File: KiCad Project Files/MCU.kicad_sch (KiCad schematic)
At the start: 25 parts, among them SW1 Boot, SW2 Reset, U1 RP2040, U2 W25Q128JVS, Y1 12MHz

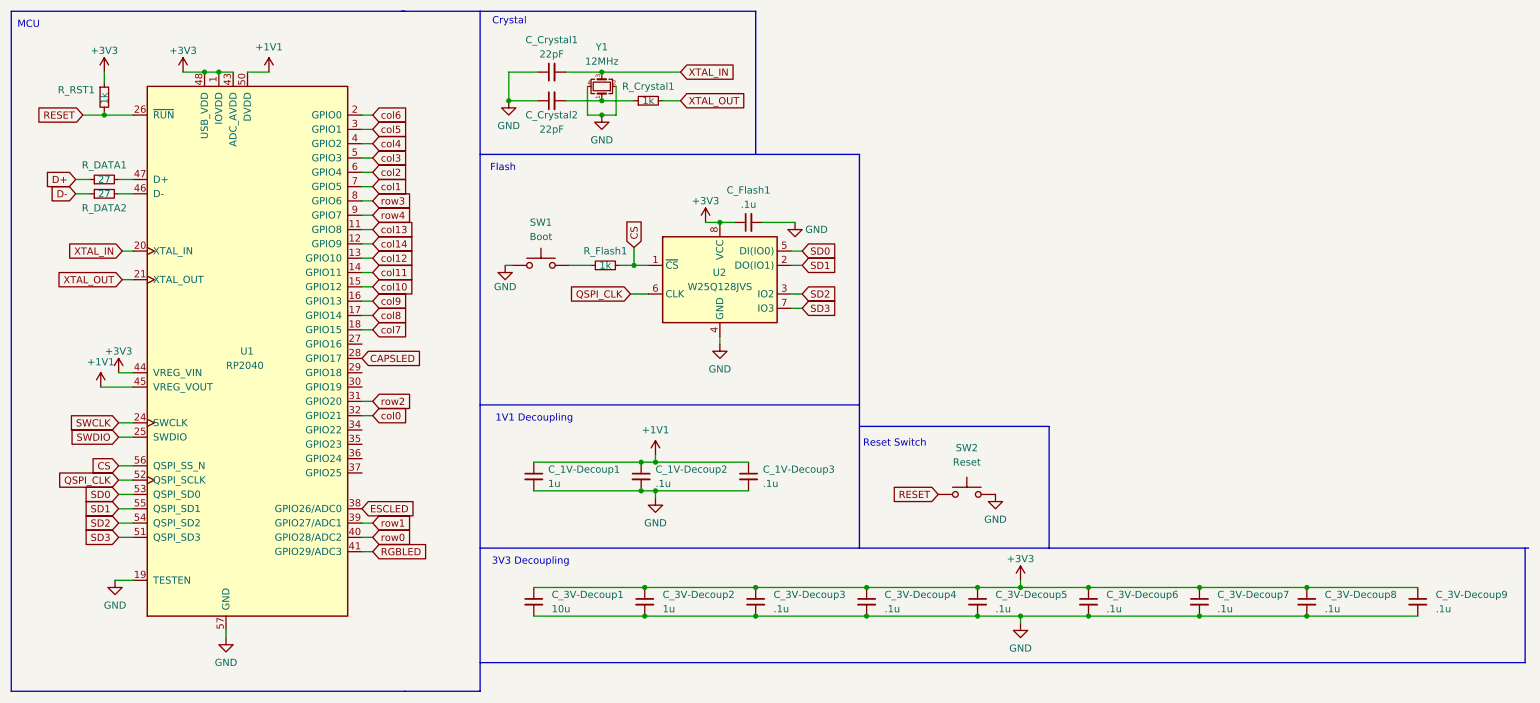
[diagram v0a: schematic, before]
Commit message: Initial Modifications
Summary of changes from original SST60:
-Removes extraneous keys, opting for ANSI-only, split right shift, split Backspace, 7U space bar, stepped caps lock.
-Switched from MX-ANSI hybrid to MX-only
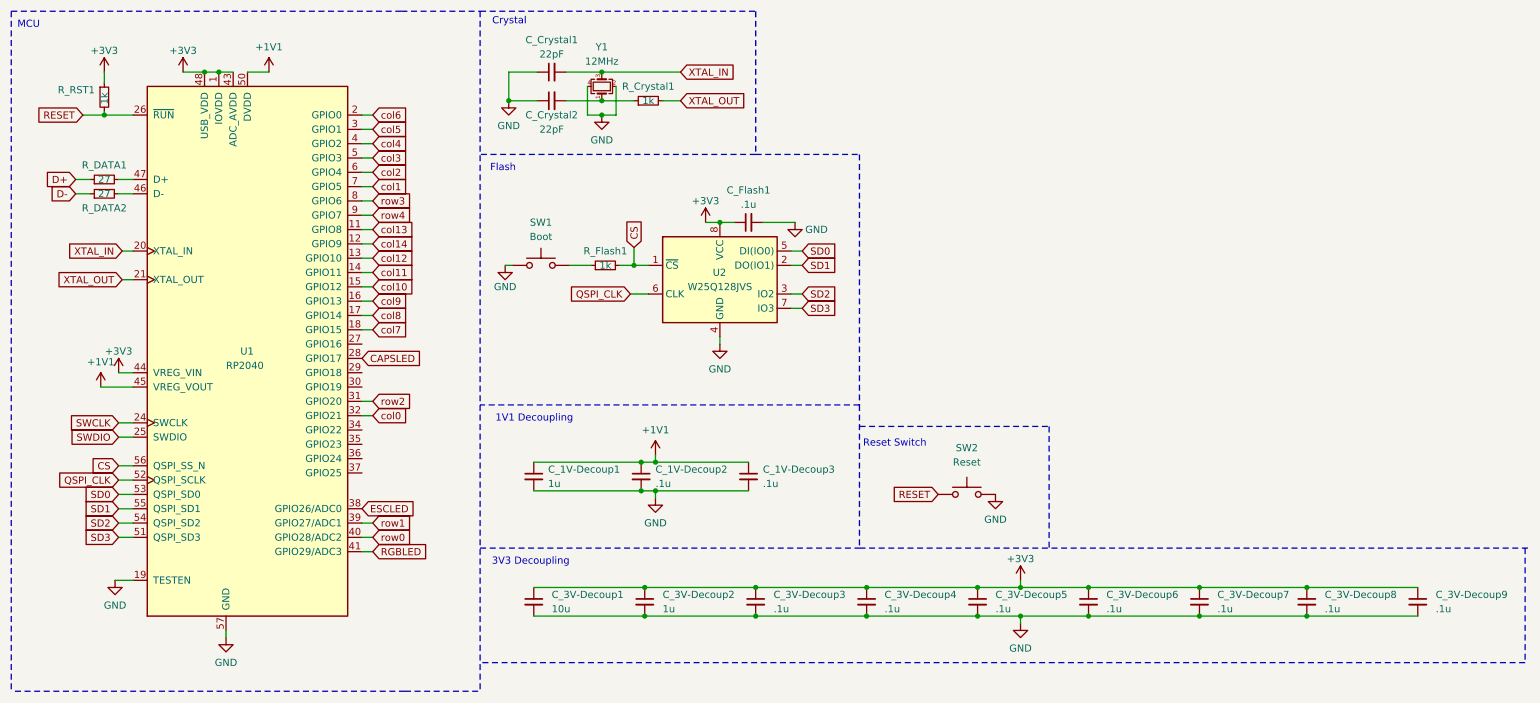
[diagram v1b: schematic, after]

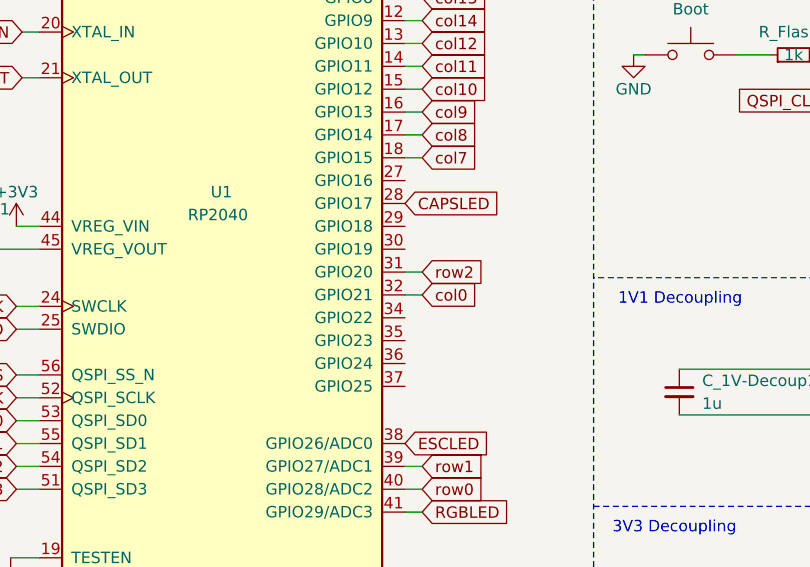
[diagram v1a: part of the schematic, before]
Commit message: Error Cleanup
Resolved all errors in sch, and most errors in pcb, except "intentional" ones concerning H1.
Will readdress rule changes and violations once attempting to submit to fab house.
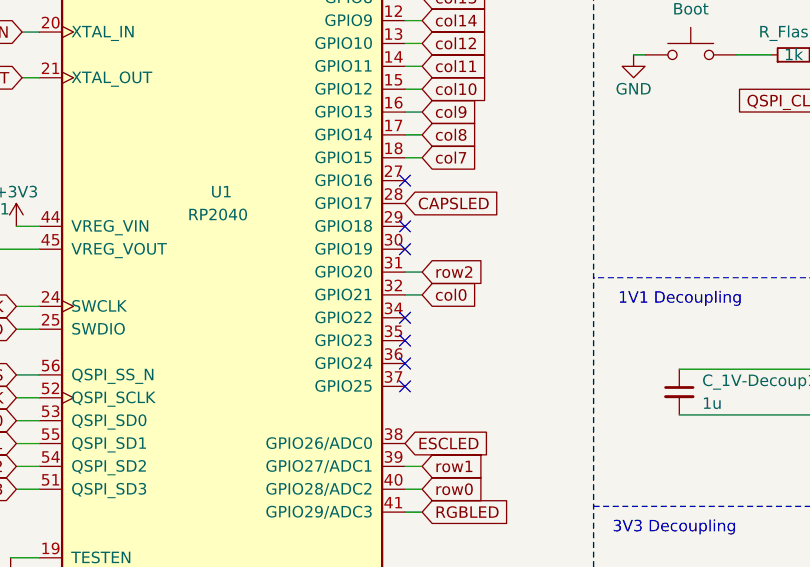
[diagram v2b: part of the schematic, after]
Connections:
- no-connect marks 0 -> 7
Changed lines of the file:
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@@
 		(color 0 0 0 0)
+	)
+	(no_connect
+		(at 74.93 92.075)
+	)
+	(no_connect
+		(at 74.93 71.755)
+	)
+	(no_connect
+		(at 74.93 76.835)
+	)
+	(no_connect
+		(at 74.93 86.995)
+	)
+	(no_connect
+		(at 74.93 79.375)
+	)
+	(no_connect
+		(at 74.93 89.535)
+	)
+	(no_connect
+		(at 74.93 94.615)
 	)
 	(polyline

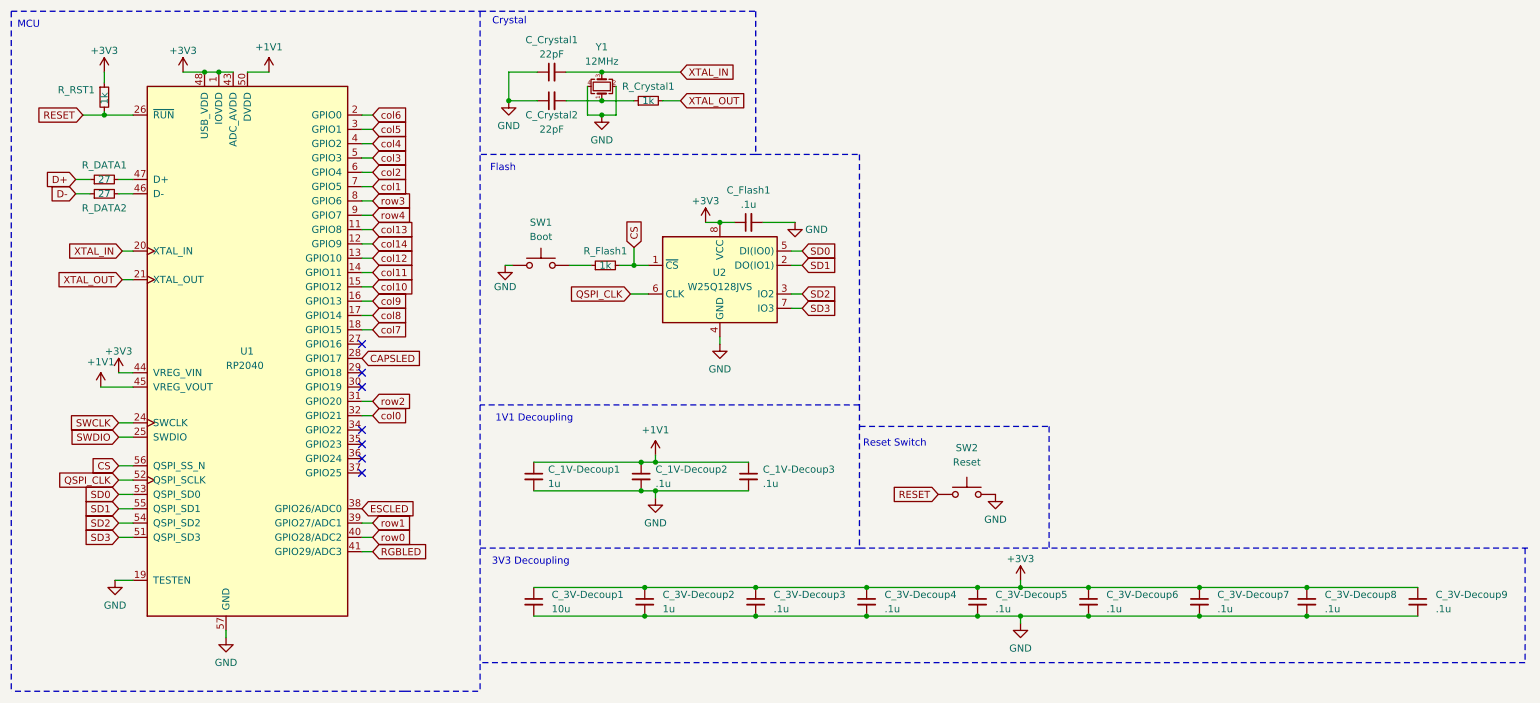
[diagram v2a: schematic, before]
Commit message: Component updates
Updates to components to facilitate JLC PCB process.
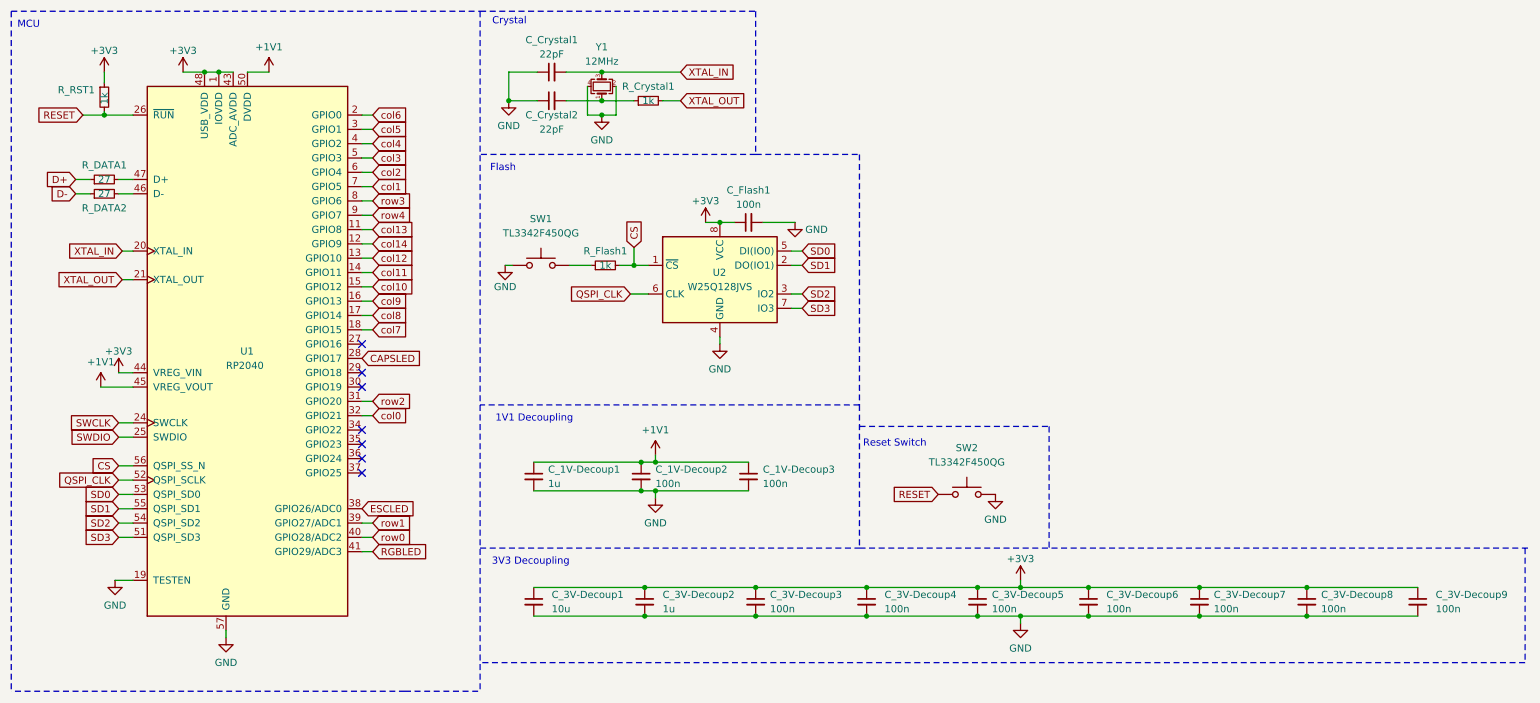
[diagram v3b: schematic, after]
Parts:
- C_1V-Decoup2, C_1V-Decoup3, C_3V-Decoup3, C_3V-Decoup4, C_3V-Decoup5, C_3V-Decoup6, C_3V-Decoup7, C_3V-Decoup8, C_3V-Decoup9, C_Flash1: value .1u -> 100n
- SW1: value Boot -> TL3342F450QG
- SW2: value Reset -> TL3342F450QG
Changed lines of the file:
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@@
 		(fields_autoplaced yes)
 		(property "Reference" "C_3V-Decoup5"
-			(at 187.325 116.2112 0)
-			(effects
-				(font
-					(size 1.27 1.27)
-				)
-				(justify left)
-			)
-		)
-		(property "Value" ".1u"
-			(at 187.325 118.7512 0)
+			(at 186.69 116.2112 0)
+			(effects
+				(font
+					(size 1.27 1.27)
+				)
+				(justify left)
+			)
+		)
+		(property "Value" "100n"
+			(at 186.69 118.7512 0)
 			(effects
 				(font
@@
 			)
 		)
-		(property "Value" ".1u"
+		(property "Value" "100n"
 			(at 127 96.5262 0)
 			(effects
@@
 		(fields_autoplaced yes)
 		(property "Reference" "C_3V-Decoup8"
-			(at 245.745 116.2112 0)
-			(effects
-				(font
-					(size 1.27 1.27)
-				)
-				(justify left)
-			)
-		)
-		(property "Value" ".1u"
-			(at 245.745 118.7512 0)
+			(at 245.11 116.2112 0)
+			(effects
+				(font
+					(size 1.27 1.27)
+				)
+				(justify left)
+			)
+		)
+		(property "Value" "100n"
+			(at 245.11 118.7512 0)
 			(effects
 				(font
@@
 			)
 		)
-		(property "Value" "Reset"
+		(property "Value" "TL3342F450QG"
 			(at 182.245 92.71 0)
 			(effects
@@
 			)
 		)
-		(property "Description" ""
+		(property "Description" "Reset"
 			(at 182.245 98.425 0)
 			(effects
@@
 			)
 		)
-		(property "Value" ".1u"
+		(property "Value" "100n"
 			(at 167.64 118.7512 0)
 			(effects
@@
 		(fields_autoplaced yes)
 		(property "Reference" "SW1"
-			(at 106.68 50.165 0)
-			(effects
-				(font
-					(size 1.27 1.27)
-				)
-			)
-		)
-		(property "Value" "Boot"
-			(at 106.68 52.705 0)
+			(at 106.68 49.53 0)
+			(effects
+				(font
+					(size 1.27 1.27)
+				)
+			)
+		)
+		(property "Value" "TL3342F450QG"
+			(at 106.68 52.07 0)
 			(effects
 				(font
@@
 			)
 		)
-		(property "Description" ""
+		(property "Description" "Boot"
 			(at 106.68 57.785 0)
 			(effects
@@
 			)
 		)
-		(property "Value" ".1u"
+		(property "Value" "100n"
 			(at 146.05 96.5262 0)
 			(effects
@@
 		(fields_autoplaced yes)
 		(property "Reference" "C_3V-Decoup7"
-			(at 226.695 116.2112 0)
-			(effects
-				(font
-					(size 1.27 1.27)
-				)
-				(justify left)
-			)
-		)
-		(property "Value" ".1u"
-			(at 226.695 118.7512 0)
+			(at 226.06 116.2112 0)
+			(effects
+				(font
+					(size 1.27 1.27)
+				)
+				(justify left)
+			)
+		)
+		(property "Value" "100n"
+			(at 226.06 118.7512 0)
 			(effects
 				(font
@@
 			)
 		)
-		(property "Value" ".1u"
+		(property "Value" "100n"
 			(at 265.43 118.7512 0)
 			(effects
@@
 			)
 		)
-		(property "Value" ".1u"
+		(property "Value" "100n"
 			(at 207.01 118.7512 0)
 			(effects
@@
 		(fields_autoplaced yes)
 		(property "Reference" "C_3V-Decoup3"
-			(at 147.955 116.2112 0)
-			(effects
-				(font
-					(size 1.27 1.27)
-				)
-				(justify left)
-			)
-		)
-		(property "Value" ".1u"
-			(at 147.955 118.7512 0)
+			(at 147.32 116.2112 0)
+			(effects
+				(font
+					(size 1.27 1.27)
+				)
+				(justify left)
+			)
+		)
+		(property "Value" "100n"
+			(at 147.32 118.7512 0)
 			(effects
 				(font
@@
 			)
 		)
-		(property "Value" ".1u"
+		(property "Value" "100n"
 			(at 143.51 46.99 90)
 			(effects
